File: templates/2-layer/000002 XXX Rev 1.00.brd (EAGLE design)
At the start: 242 x 230 mm, 20 parts, among them X1 PAD_TEST_GROUND_HOOK

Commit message: 2-layer template
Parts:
- added ART2: ART_SN_LABEL-08X24, Custom_Eagle_KD:ART_SN_8X24
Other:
- board text added: ">PCB_PN"
- board text removed: ">PRODUCT_NUMBER"
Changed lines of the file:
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@@
 <?xml version="1.0" encoding="utf-8"?>
 <!DOCTYPE eagle SYSTEM "eagle.dtd">
-<eagle version="9.4.2">
+<eagle version="9.6.2">
 <drawing>
 <settings>
@@
 <layers>
 <layer number="1" name="Top" color="4" fill="1" visible="yes" active="yes"/>
+<layer number="2" name="Route2" color="1" fill="3" visible="no" active="no"/>
+<layer number="3" name="Route3" color="4" fill="3" visible="no" active="no"/>
+<layer number="4" name="Route4" color="1" fill="4" visible="no" active="no"/>
+<layer number="5" name="Route5" color="4" fill="4" visible="no" active="no"/>
+<layer number="6" name="Route6" color="1" fill="8" visible="no" active="no"/>
+<layer number="7" name="Route7" color="4" fill="8" visible="no" active="no"/>
+<layer number="8" name="Route8" color="1" fill="2" visible="no" active="no"/>
+<layer number="9" name="Route9" color="4" fill="2" visible="no" active="no"/>
+<layer number="10" name="Route10" color="1" fill="7" visible="no" active="no"/>
+<layer number="11" name="Route11" color="4" fill="7" visible="no" active="no"/>
+<layer number="12" name="Route12" color="1" fill="5" visible="no" active="no"/>
+<layer number="13" name="Route13" color="4" fill="5" visible="no" active="no"/>
+<layer number="14" name="Route14" color="1" fill="6" visible="no" active="no"/>
+<layer number="15" name="Route15" color="4" fill="6" visible="no" active="no"/>
 <layer number="16" name="Bottom" color="1" fill="1" visible="yes" active="yes"/>
 <layer number="17" name="Pads" color="2" fill="1" visible="yes" active="yes"/>
@@
 <layer number="25" name="tNames" color="7" fill="1" visible="yes" active="yes"/>
 <layer number="26" name="bNames" color="11" fill="1" visible="yes" active="yes"/>
-<layer number="27" name="tValues" color="7" fill="1" visible="no" active="yes"/>
+<layer number="27" name="tValues" color="7" fill="1" visible="yes" active="yes"/>
 <layer number="28" name="bValues" color="7" fill="1" visible="no" active="yes"/>
 <layer number="29" name="tStop" color="7" fill="3" visible="yes" active="yes"/>
@@
 <wire x1="100" y1="80" x2="0" y2="80" width="0" layer="20"/>
 <wire x1="0" y1="80" x2="0" y2="0" width="0" layer="20"/>
-<dimension x1="100" y1="80" x2="0" y2="80" x3="50" y3="95" textsize="1" textratio="12" layer="48" dtype="horizontal"/>
-<dimension x1="100" y1="0" x2="100" y2="80" x3="115" y3="40" textsize="1" textratio="12" layer="48" dtype="vertical"/>
+<dimension x1="100" y1="80" x2="0" y2="80" x3="50" y3="95" textsize="1" textratio="12" layer="46" dtype="horizontal"/>
+<dimension x1="100" y1="0" x2="100" y2="80" x3="115" y3="40" textsize="1" textratio="12" layer="46" dtype="vertical"/>
 <text x="-38" y="39" size="1" layer="21" font="vector" ratio="12">&gt;DATE</text>
 <text x="-36" y="37" size="1" layer="21" font="vector" ratio="12" align="bottom-right">&gt;REVISION</text>
@@
 <text x="152.5" y="11" size="2.5" layer="20" font="vector" ratio="12" align="top-left">&gt;REVISION</text>
 <text x="134" y="16" size="2.5" layer="20" font="vector" ratio="12" align="top-left">PN: </text>
-<text x="141" y="16" size="2.5" layer="20" font="vector" ratio="12" align="top-left">&gt;PRODUCT_NUMBER</text>
-<text x="-34" y="37" size="1" layer="21" font="vector" ratio="12">&gt;PRODUCT_NUMBER</text>
+<text x="141" y="16" size="2.5" layer="20" font="vector" ratio="12" align="top-left">&gt;PCB_PN</text>
+<text x="-34" y="37" size="1" layer="21" font="vector" ratio="12">&gt;PCB_PN</text>
 <text x="-35" y="37" size="1" layer="21" font="vector" ratio="12" rot="MR0">|</text>
 <text x="134" y="26" size="2.5" layer="46" font="vector" ratio="12" align="top-left">Drill drawing</text>
@@
 <attribute name="DATE" value="25.2.2018"/>
 <attribute name="OWNER" value="Kallio Designs"/>
-<attribute name="PRODUCT_NUMBER" value="XXXX"/>
+<attribute name="PCB_PN" value="XXXX"/>
 <attribute name="REVISION" value="1.0"/>
 </attributes>
@@
 <attribute name="SUPPLIER_PARTNO" value="DNP" x="-37" y="-42" size="1" layer="27" font="vector" ratio="12" display="off"/>
 </element>
+<element name="ART2" library="Custom_Eagle_KD" package="ART_SN_8X24" value="ART_SN_LABEL-08X24" x="-38" y="-52" smashed="yes">
+<attribute name="CODE" value="SN Label" x="-38" y="-52" size="1" layer="27" font="vector" ratio="12" display="off"/>
+<attribute name="DNP" value="T" x="-38" y="-52" size="1" layer="27" font="vector" ratio="12" display="off"/>
+<attribute name="MANUFACTURER" value="DNP" x="-38" y="-52" size="1" layer="27" font="vector" ratio="12" display="off"/>
+<attribute name="MFG_PARTNO" value="DNP" x="-38" y="-52" size="1" layer="27" font="vector" ratio="12" display="off"/>
+<attribute name="PRICE" value="0" x="-38" y="-52" size="1" layer="27" font="vector" ratio="12" display="off"/>
+<attribute name="SUPPLIER" value="Digi-Key" x="-38" y="-52" size="1" layer="27" font="vector" ratio="12" display="off"/>
+<attribute name="SUPPLIER_PARTNO" value="DNP" x="-38" y="-52" size="1" layer="27" font="vector" ratio="12" display="off"/>
+</element>
 </elements>

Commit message: Template updates
For syncing with fusion
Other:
- board size 242 x 230 mm -> 130 x 230 mm
- board text added: "Board outline"
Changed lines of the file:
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@@
 <layers>
 <layer number="1" name="Top" color="4" fill="1" visible="yes" active="yes"/>
-<layer number="2" name="Route2" color="1" fill="3" visible="no" active="no"/>
-<layer number="3" name="Route3" color="4" fill="3" visible="no" active="no"/>
-<layer number="4" name="Route4" color="1" fill="4" visible="no" active="no"/>
-<layer number="5" name="Route5" color="4" fill="4" visible="no" active="no"/>
-<layer number="6" name="Route6" color="1" fill="8" visible="no" active="no"/>
-<layer number="7" name="Route7" color="4" fill="8" visible="no" active="no"/>
-<layer number="8" name="Route8" color="1" fill="2" visible="no" active="no"/>
-<layer number="9" name="Route9" color="4" fill="2" visible="no" active="no"/>
-<layer number="10" name="Route10" color="1" fill="7" visible="no" active="no"/>
-<layer number="11" name="Route11" color="4" fill="7" visible="no" active="no"/>
-<layer number="12" name="Route12" color="1" fill="5" visible="no" active="no"/>
-<layer number="13" name="Route13" color="4" fill="5" visible="no" active="no"/>
-<layer number="14" name="Route14" color="1" fill="6" visible="no" active="no"/>
-<layer number="15" name="Route15" color="4" fill="6" visible="no" active="no"/>
 <layer number="16" name="Bottom" color="1" fill="1" visible="yes" active="yes"/>
 <layer number="17" name="Pads" color="2" fill="1" visible="yes" active="yes"/>
@@
 <layer number="25" name="tNames" color="7" fill="1" visible="yes" active="yes"/>
 <layer number="26" name="bNames" color="11" fill="1" visible="yes" active="yes"/>
-<layer number="27" name="tValues" color="7" fill="1" visible="yes" active="yes"/>
+<layer number="27" name="tValues" color="7" fill="1" visible="no" active="yes"/>
 <layer number="28" name="bValues" color="7" fill="1" visible="no" active="yes"/>
 <layer number="29" name="tStop" color="7" fill="3" visible="yes" active="yes"/>
@@
 <layer number="97" name="Info" color="7" fill="1" visible="no" active="no"/>
 <layer number="98" name="Guide" color="6" fill="1" visible="no" active="no"/>
+<layer number="2" name="Route2" color="1" fill="3" visible="no" active="no"/>
+<layer number="3" name="Route3" color="4" fill="3" visible="no" active="no"/>
+<layer number="4" name="Route4" color="1" fill="4" visible="no" active="no"/>
+<layer number="5" name="Route5" color="4" fill="4" visible="no" active="no"/>
+<layer number="6" name="Route6" color="1" fill="8" visible="no" active="no"/>
+<layer number="7" name="Route7" color="4" fill="8" visible="no" active="no"/>
+<layer number="8" name="Route8" color="1" fill="2" visible="no" active="no"/>
+<layer number="9" name="Route9" color="4" fill="2" visible="no" active="no"/>
+<layer number="10" name="Route10" color="1" fill="7" visible="no" active="no"/>
+<layer number="11" name="Route11" color="4" fill="7" visible="no" active="no"/>
+<layer number="12" name="Route12" color="1" fill="5" visible="no" active="no"/>
+<layer number="13" name="Route13" color="4" fill="5" visible="no" active="no"/>
+<layer number="14" name="Route14" color="1" fill="6" visible="no" active="no"/>
+<layer number="15" name="Route15" color="4" fill="6" visible="no" active="no"/>
 <layer number="53" name="tGND_GNDA" color="7" fill="9" visible="no" active="no"/>
 <layer number="54" name="bGND_GNDA" color="1" fill="9" visible="no" active="no"/>
@@
 <text x="-36" y="37" size="1" layer="21" font="vector" ratio="12" align="bottom-right">&gt;REVISION</text>
 <text x="134" y="26" size="2.5" layer="1" font="vector" ratio="12" align="top-left">TOP LAYER</text>
-<text x="134" y="11" size="2.5" layer="20" font="vector" ratio="12" align="top-left">PCB Rev: </text>
+<text x="134" y="11" size="2.5" layer="48" font="vector" ratio="12" align="top-left">PCB Rev: </text>
 <text x="134" y="26" size="2.5" layer="16" font="vector" ratio="12" align="top-left">BOTTOM LAYER</text>
 <wire x1="3" y1="230" x2="99" y2="230" width="0.5" layer="46"/>
@@
 <wire x1="130" y1="194" x2="130" y2="188" width="0.5" layer="46"/>
 <wire x1="130" y1="188" x2="130" y2="182" width="0.5" layer="46"/>
-<wire x1="130" y1="182" x2="130" y2="176" width="0.5" layer="46"/>
-<wire x1="130" y1="176" x2="130" y2="110" width="0.5" layer="46"/>
+<wire x1="130" y1="182" x2="130" y2="110" width="0.5" layer="46"/>
 <wire x1="130" y1="110" x2="3" y2="110" width="0.5" layer="46"/>
 <wire x1="3" y1="110" x2="3" y2="176" width="0.5" layer="46"/>
@@
 <text x="134" y="23" size="2.5" layer="31" font="vector" ratio="12" align="top-left">Paste mask top</text>
 <text x="134" y="23" size="2.5" layer="32" font="vector" ratio="12" align="top-left">Paste mask bottom</text>
-<wire x1="132" y1="28" x2="242" y2="28" width="0.5" layer="20"/>
-<wire x1="242" y1="28" x2="242" y2="1" width="0.5" layer="20"/>
-<wire x1="242" y1="1" x2="132" y2="1" width="0.5" layer="20"/>
-<wire x1="132" y1="1" x2="132" y2="28" width="0.5" layer="20"/>
-<text x="134" y="6" size="2.5" layer="20" font="vector" ratio="12" align="top-left">&gt;OWNER</text>
-<text x="240" y="6" size="2.5" layer="20" font="vector" ratio="12" align="top-right">&gt;DATE</text>
-<text x="152.5" y="11" size="2.5" layer="20" font="vector" ratio="12" align="top-left">&gt;REVISION</text>
-<text x="134" y="16" size="2.5" layer="20" font="vector" ratio="12" align="top-left">PN: </text>
-<text x="141" y="16" size="2.5" layer="20" font="vector" ratio="12" align="top-left">&gt;PCB_PN</text>
+<wire x1="132" y1="28" x2="242" y2="28" width="0.5" layer="48"/>
+<wire x1="242" y1="28" x2="242" y2="1" width="0.5" layer="48"/>
+<wire x1="242" y1="1" x2="132" y2="1" width="0.5" layer="48"/>
+<wire x1="132" y1="1" x2="132" y2="28" width="0.5" layer="48"/>
+<text x="134" y="6" size="2.5" layer="48" font="vector" ratio="12" align="top-left">&gt;OWNER</text>
+<text x="240" y="6" size="2.5" layer="48" font="vector" ratio="12" align="top-right">&gt;DATE</text>
+<text x="152.5" y="11" size="2.5" layer="48" font="vector" ratio="12" align="top-left">&gt;REVISION</text>
+<text x="134" y="16" size="2.5" layer="48" font="vector" ratio="12" align="top-left">PN: </text>
+<text x="141" y="16" size="2.5" layer="48" font="vector" ratio="12" align="top-left">&gt;PCB_PN</text>
 <text x="-34" y="37" size="1" layer="21" font="vector" ratio="12">&gt;PCB_PN</text>
 <text x="-35" y="37" size="1" layer="21" font="vector" ratio="12" rot="MR0">|</text>
@@
 <text x="101" y="210" size="2.5" layer="46" font="vector" ratio="12" align="top-left">Order form</text>
 <text x="101" y="204" size="2.5" layer="46" font="vector" ratio="12" align="top-left">Order form</text>
+<text x="134" y="26" size="2.5" layer="20" font="vector" ratio="12" align="top-left">Board outline</text>
 </plain>
 <attributes>

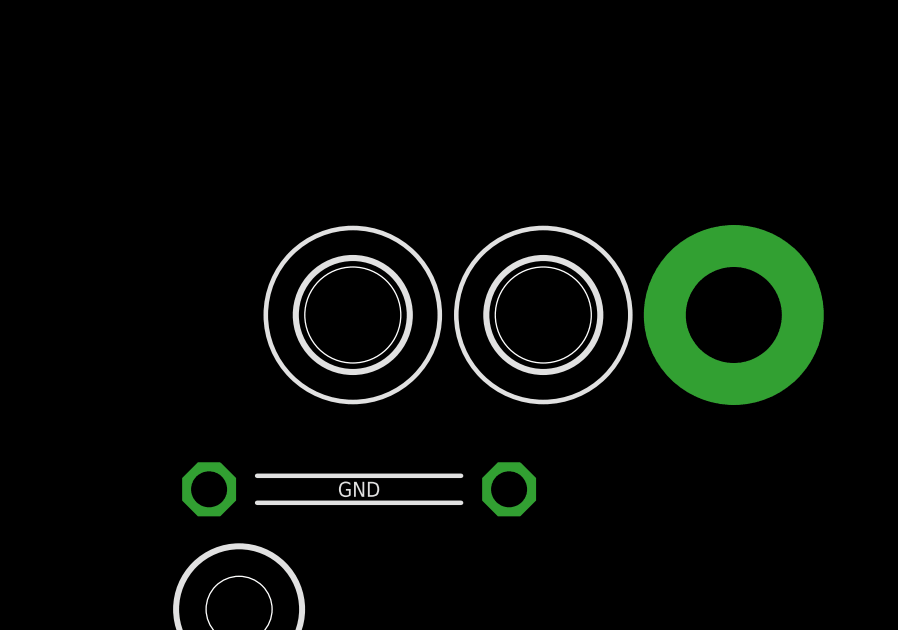
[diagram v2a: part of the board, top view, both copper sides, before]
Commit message: Changed templates to managed libraries
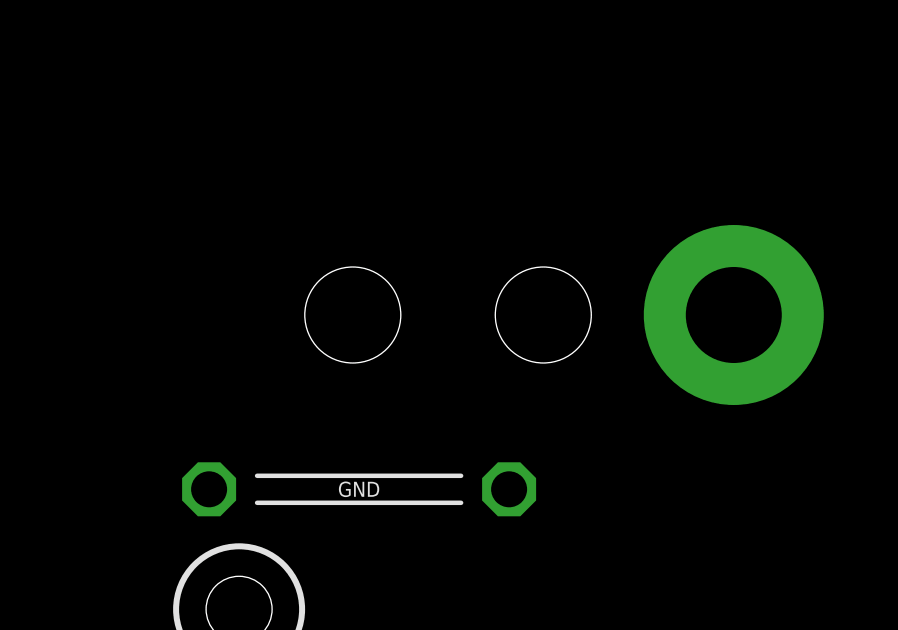
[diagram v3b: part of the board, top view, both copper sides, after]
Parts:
- MTG5, MTG6: value HOL_3.2/6.0_NP -> HOL_3.2/6.0_NP-NOSILK; device Custom_Eagle_KD:MTG_NP_M3_320X600 -> Custom_Eagle_KD:MTG_NP_M3_320X600_NOSILK
